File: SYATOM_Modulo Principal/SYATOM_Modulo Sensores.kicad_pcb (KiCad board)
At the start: 4 copper layers, 100 x 120 mm, 145 parts, among them J1 Input, J10 Head_HX711_2, J11 Head_HX711, J12 Exp_GPIO, J13 Exp_ADC, J14 Exp_I2C, J15 PWM_A, J16 PWM_B, J17 Header_Max485_1, J18 Header_Max3232, J19 Header_Max485_2, J2 Temp_SEN, J20 Niv_alm_SEN, J21 Vcc, J22 Optocoupler, J3 pH_SEN, J4 Oxig_SEN, J5 Nivel_SEN, J6 Turb_SEN, J7 TDS_SEN, J8 Niv_mst_SEN, J9 Nivel2_SEN, Q1 IRF3205, Q2 IRF3205, SW1 SWDIP, SW2 SW_Push, U1 LM358, U10 PC817, U11 PC817, U12 PC817, U13 PC817, U14 PC817, U15 PC817, U16 PC817, U17 PC817, U18 PC817, U19 TPS2041B, U2 LM358, U20 TPS2041B, U21 TPS2041B, U22 TPS2041B, U23 LM7805_TO220, U3 LM358, U4 LM358, U5 LM358, U7 LM7805_TO220, U8 MIC4427, U9 PC817

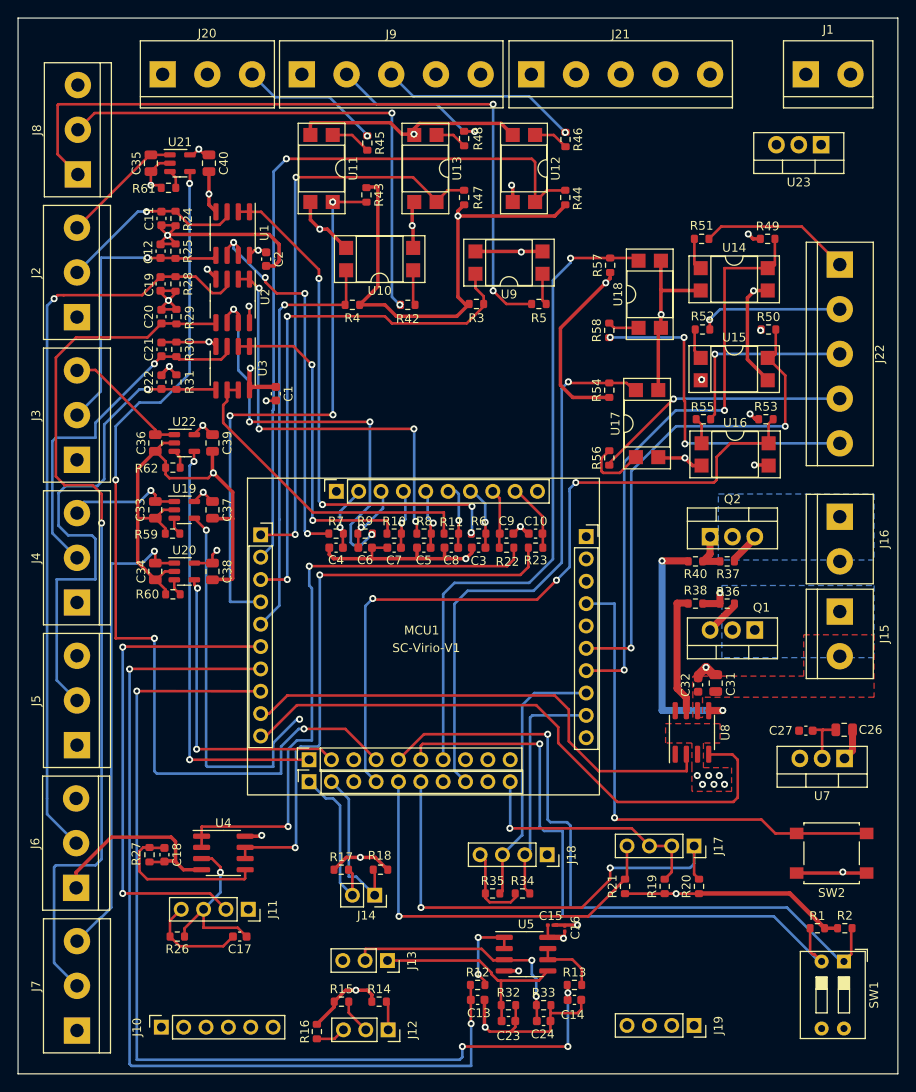
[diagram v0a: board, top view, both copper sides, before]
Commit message: Add files via upload
Se agrego el silkscreen de los logos y label de los conectores, ademas una resistencia pull-up al botón reset
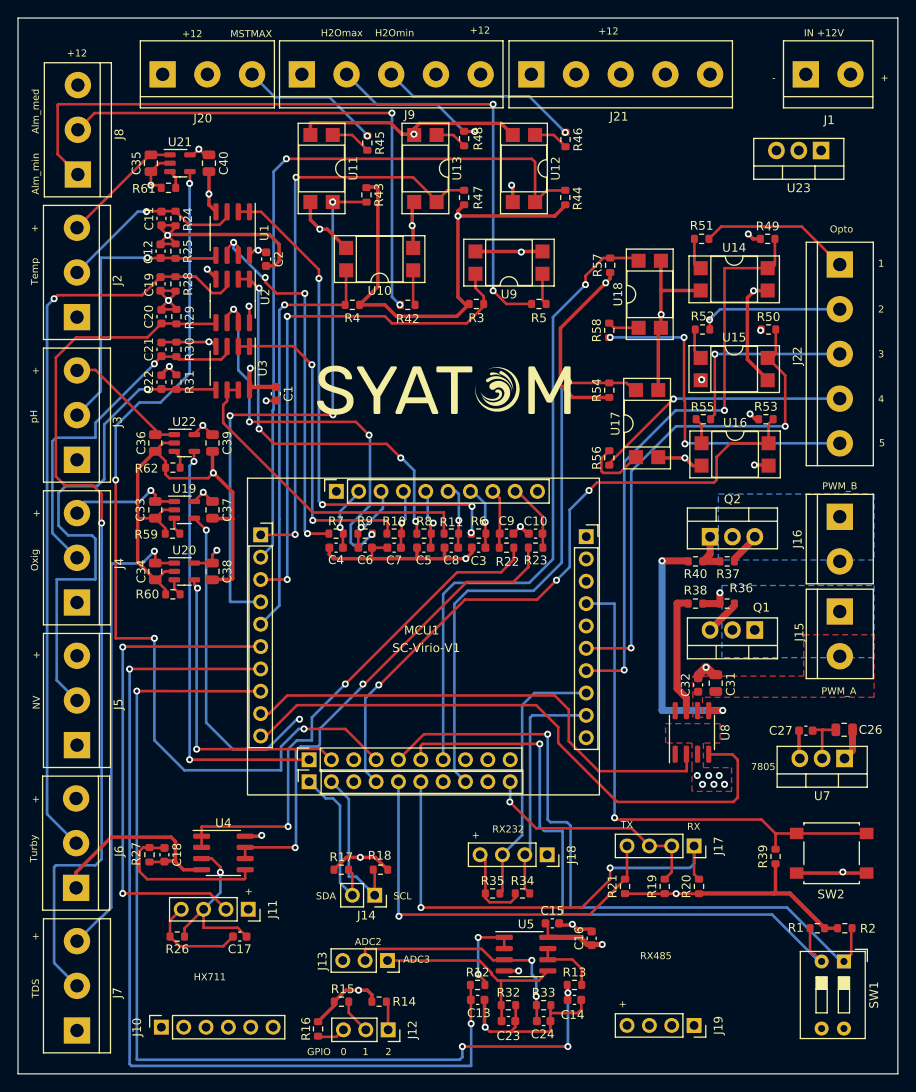
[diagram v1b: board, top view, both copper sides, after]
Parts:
- added G***: LOGO, SYATOM logo:pecadito, B.Cu at (136.8, 83.3)
- added GE: LOGO, SYATOM logo:Isologo_SYATOM, F.Cu at (118.3, 91.6)
- added GE: LOGO, SYATOM logo:Isologo_SYATOM, B.Cu at (136.9, 154.9)
- added R39: 10k, Resistor_SMD:R_0603_1608Metric, F.Cu at (155.8, 145.0)
- C15, C16: footprint Capacitor_SMD:C_0201_0603Metric -> Capacitor_SMD:C_0603_1608Metric
- SW2: value SW_Push -> SW_Reset
- moved C16 3.25 mm to (134.9, 154.3)
- moved U23 0.66 mm to (161.0, 64.8)
- moved R16 0.33 mm to (103.8, 164.6)
- moved C15 0.27 mm to (130.4, 152.6)
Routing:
- net Net-(R22-Pad2): track 68.9 -> 58.4 mm
- net Net-(R23-Pad2): track 66.6 -> 56.4 mm
- net /Opto3_ext: track 83.8 -> 76.1 mm
- net /Act_Sensor_Oxig: track 52.0 -> 45.9 mm
- net +5V: track 105.0 -> 108.9 mm
- net +3V3: track 159.7 -> 162.8 mm
- net Net-(R8-Pad2): track 48.5 -> 45.8 mm
- net /Act_Sensor_Temp: track 108.1 -> 105.5 mm
- net /Opto5_ext: track 75.8 -> 73.7 mm
- net /Rest: track 56.9 -> 58.8 mm
- net ENA_485_GPIO: track 28.7 -> 26.9 mm
- net GND: track 316.9 -> 318.5 mm
- net Net-(R9-Pad2): track 48.4 -> 47.5 mm
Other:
- board text added: "+"
- board text added: "+12"
- board text added: "-"
- board text added: "0"
- board text added: "1"
- board text added: "2"
- board text added: "3"
- board text added: "4"
- board text added: "5"
- board text added: "7805"
- board text added: "ADC2"
- board text added: "ADC3"
- board text added: "Alm_med"
- board text added: "Alm_min"
- board text added: "GPIO"
- board text added: "H2Omax"
- board text added: "H2Omin"
- board text added: "HX711"
- board text added: "IN +12V"
- board text added: "MSTMAX"
- board text added: "NV"
- board text added: "Opto"
- board text added: "Oxig"
- board text added: "PWM_A"
- board text added: "PWM_B"
- board text added: "RX"
- board text added: "RX232"
- board text added: "RX485"
- board text added: "SCL"
- board text added: "SDA"
- board text added: "TDS"
- board text added: "TX"
- board text added: "Temp"
- board text added: "Turby"
- board text added: "pH"
